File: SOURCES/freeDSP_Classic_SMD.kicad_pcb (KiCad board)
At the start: 2 copper layers, 173 parts, among them J1 RCA_01, J2 RCA_01, J3 CONN_01X02, J4 RCA_01, J5 RCA_01, J6 RCA_01, J7 RCA_01, P1 CONN_01X06, P2 CONN_01X03, P3 CONN_02X05, P4 STDCONN, P5 STDCONN, P6 STDCONN, P7 STDCONN, P8 CONN_02X03, P9 CONN_02X03, Q1 BSS123, Q10 BSH103,215, Q11 BSH103,215, Q12 BSH103,215, Q13 BSH103,215, Q14 MMBF5434, Q15 MMBF5434, Q16 MMBF5434, Q17 MMBF5434, Q18 BSS123, Q2 BSS123, Q3 BSS123, Q4 BSS123, Q5 FZT751TA, Q6 BSH103,215, Q7 BSH103,215, Q8 BSH103,215, Q9 BSH103,215, SW1 SW_PUSH, U1 ADAU1701, U2 24AA256SN, U3 LME49721, U4 LME49721, U5 SN74LVC3G14, U6 LM393, U7 IDT2305NZ, X1 ASV-24.576MHz-EJ-T

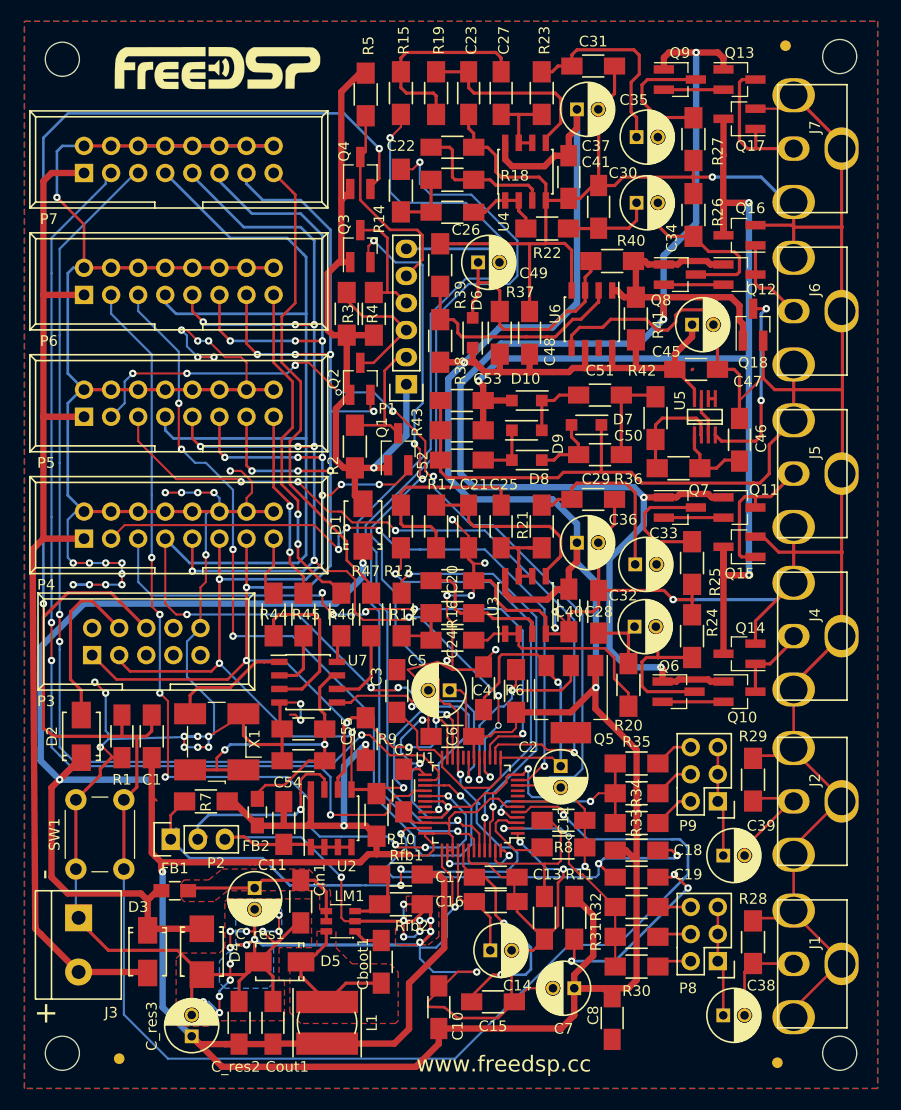
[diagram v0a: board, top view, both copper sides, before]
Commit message: added power led, changed via drill size
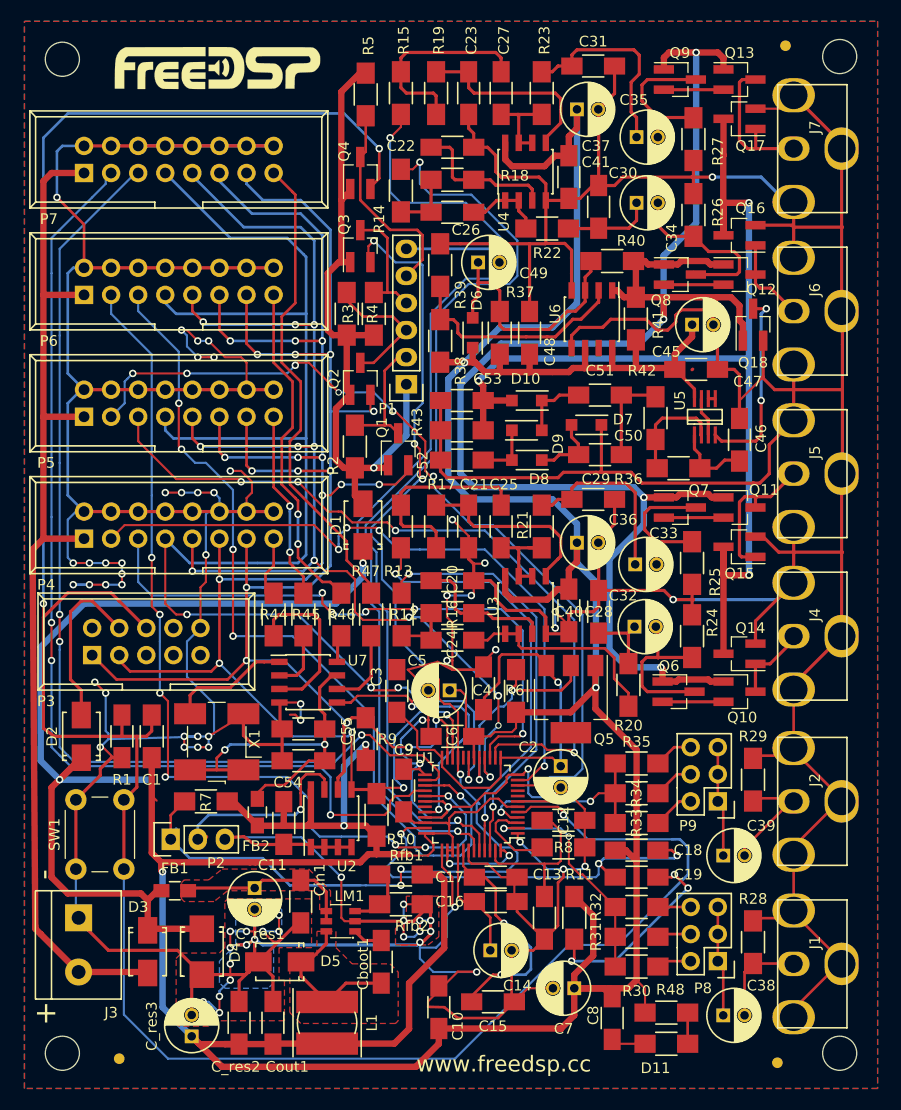
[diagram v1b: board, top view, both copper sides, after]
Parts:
- added D11: LED, fdsp_resistor:R_1206_HandSoldering, F.Cu at (123.7, 153.8)
- added R48: 330, fdsp_resistor:R_1206_HandSoldering, F.Cu at (123.7, 150.9)
- R11: value 475R -> 475
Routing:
- net +3V3: track 422.4 -> 425.7 mm
- net GND: track 1016.5 -> 1019.7 mm
- net Net-(D11-Pad2): track 0.00 -> 2.92 mm
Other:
- net class ADAU: via_drill 0.3 -> 0.4
- net class Default: via_drill 0.3 -> 0.4
- net class Supply: via_drill 0.3 -> 0.4
- rule via_min_size: 0.3 -> 0.4

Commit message: fixed wrong pinouts added some text
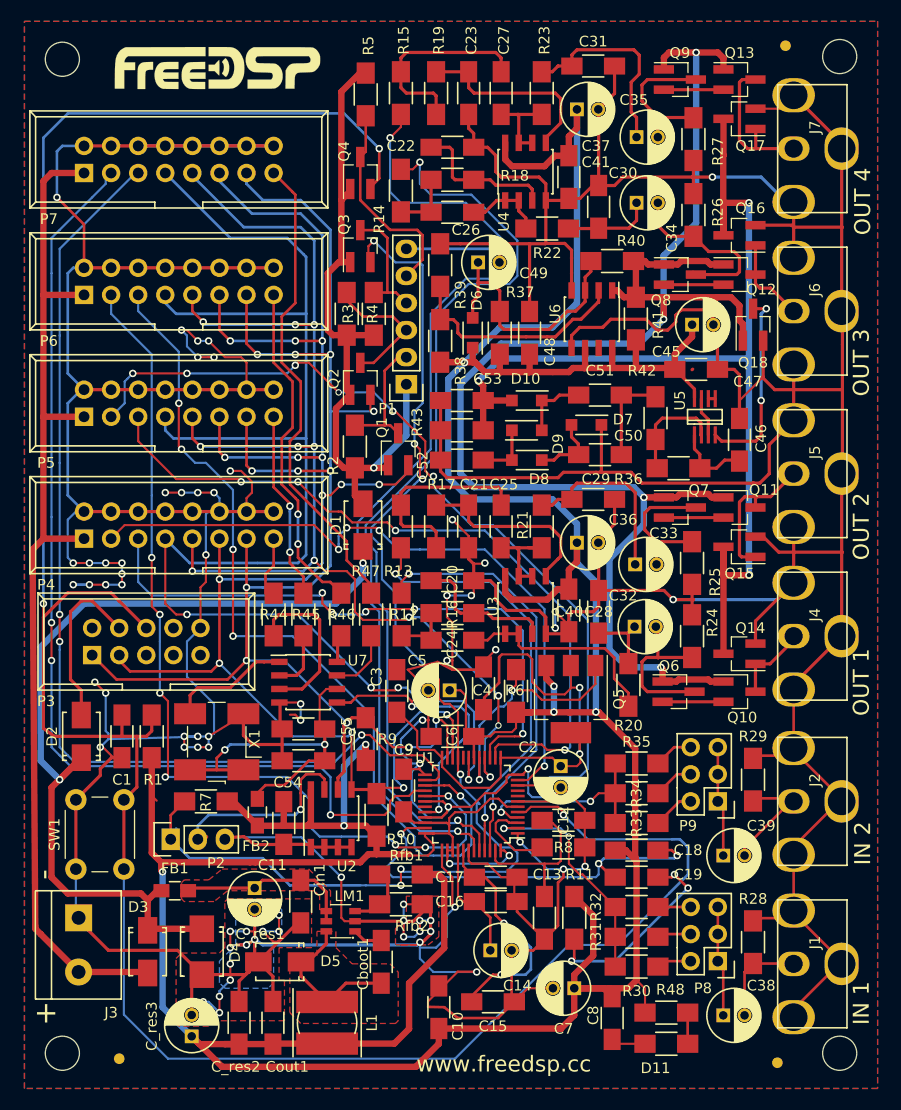
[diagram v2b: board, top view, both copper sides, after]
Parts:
- C28, C29, C30, C31: value 560p -> 5.6n
- Q5: footprint fdsp_housing_new:SOT-223 -> fdsp_housing:SOT-223
- R20, R21, R22, R23: value 2k4 -> 330
- R44, R45, R46, R47: value 33 -> 24
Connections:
- U7 pad 6: Net-(R47-Pad2) -> Net-(C54-Pad1)
- U7 pad 7: Net-(C54-Pad1) -> Net-(R47-Pad2)
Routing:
- net Net-(C2-Pad1): track 43.5 -> 53.8 mm, vias 1 -> 2
- net VIN: track 92.6 -> 84.0 mm
- net +3V3: track 425.7 -> 433.3 mm, vias 7 -> 9
- net Net-(Q5-Pad2): track 22.5 -> 25.3 mm
- net MP7: track 71.4 -> 70.3 mm
- net Net-(C54-Pad1): track 34.3 -> 33.3 mm
- net Net-(R47-Pad2): track 7.46 -> 6.64 mm
- net MP1: track 80.9 -> 81.7 mm
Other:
- board text added: "IN 1"
- board text added: "IN 2"
- board text added: "OUT 1"
- board text added: "OUT 2"
- board text added: "OUT 3"
- board text added: "OUT 4"

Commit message: Modified FZT751 Part2
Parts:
- Q5: footprint fdsp_housing:SOT-223 -> fdsp_housing_new:SOT-223
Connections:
- Q5 pad 1: +3V3 -> Net-(Q5-Pad1)
- Q5 pad 2: Net-(Q5-Pad2) -> (no net)
- Q5 pad 3: Net-(C2-Pad1) -> +3V3
- R6 pad 2: Net-(Q5-Pad2) -> Net-(Q5-Pad1)
- U1 pad 17: Net-(Q5-Pad2) -> Net-(Q5-Pad1)
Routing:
- net Net-(Q5-Pad2): track 25.3 -> 0.00 mm, vias 2 -> 0
- net Net-(Q5-Pad1): track 0.00 -> 25.3 mm, vias 0 -> 2

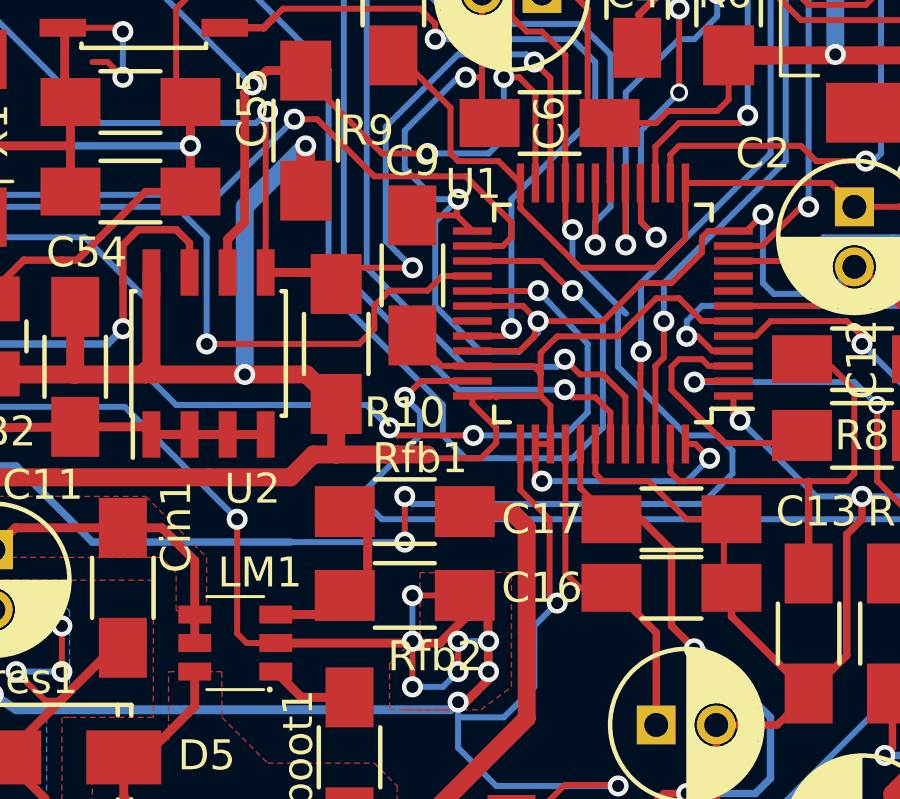
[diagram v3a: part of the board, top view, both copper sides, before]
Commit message: corrected some things in layout and schematic
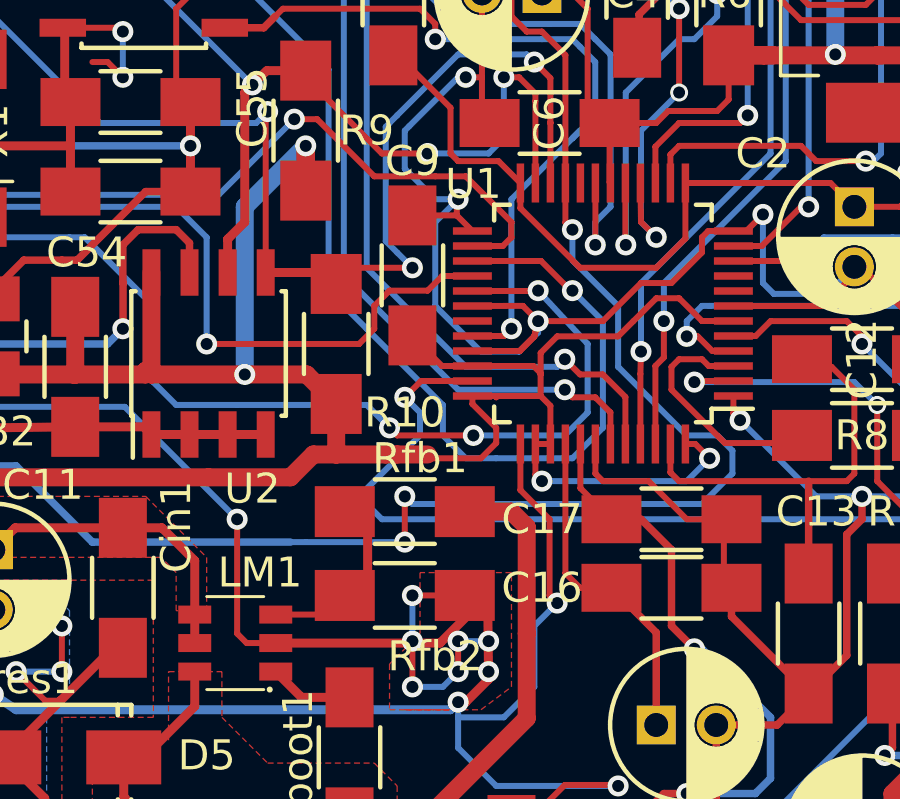
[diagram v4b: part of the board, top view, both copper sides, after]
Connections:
- Q5 pad 2: (no net) -> Net-(C2-Pad1)
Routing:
- net WP: track 115.4 -> 114.7 mm
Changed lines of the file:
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@@
-(kicad_pcb (version 4) (host pcbnew 4.0.7-e1-6374~58~ubuntu17.04.1)
+(kicad_pcb (version 4) (host pcbnew 4.0.7-e1-6374~58~ubuntu16.04.1)
   (general
-    (links 412)
+    (links 414)
     (no_connects 0)
     (area 0 0 0 0)
@@
     (pad_to_mask_clearance 0)
     (aux_axis_origin 0 0)
-    (visible_elements 7FFC0E09)
+    (visible_elements 7FFC4E0F)
     (pcbplotparams
       (layerselection 0x020c0_00000000)
@@
     (uvia_dia 0.3)
     (uvia_drill 0.1)
-    (add_net "Net-(Q5-Pad1)")
   )
   (net_class ADAU ""
@@
     (add_net "Net-(Q12-Pad2)")
     (add_net "Net-(Q13-Pad2)")
+    (add_net "Net-(Q5-Pad1)")
     (add_net "Net-(R36-Pad1)")
     (add_net "Net-(R38-Pad1)")
@@
     (fp_line (start -1.85 3.35) (end 1.85 3.35) (layer F.Fab) (width 0.1))
     (fp_line (start 1.85 -3.35) (end 1.85 3.35) (layer F.Fab) (width 0.1))
-    (pad 4 smd rect (at 3.15 0 270) (size 2 3.8) (layers F.Cu F.Paste F.Mask))
-    (pad 2 smd rect (at -3.15 0 270) (size 2 1.5) (layers F.Cu F.Paste F.Mask))
+    (pad 2 smd rect (at 3.15 0 270) (size 2 3.8) (layers F.Cu F.Paste F.Mask)
+      (net 3 "Net-(C2-Pad1)"))
+    (pad 2 smd rect (at -3.15 0 270) (size 2 1.5) (layers F.Cu F.Paste F.Mask)
+      (net 3 "Net-(C2-Pad1)"))
     (pad 3 smd rect (at -3.15 2.3 270) (size 2 1.5) (layers F.Cu F.Paste F.Mask)
       (net 4 +3V3))
@@
   (segment (start 132.08 69.85) (end 135.636 69.85) (width 0.3) (layer F.Cu) (net 52))
   (segment (start 130.556 69.088) (end 131.318 69.85) (width 0.3) (layer F.Cu) (net 52))
+  (segment (start 94.5045 141.3535) (end 96.1685 141.3535) (width 0.2) (layer F.Cu) (net 53))
+  (segment (start 96.1685 141.3535) (end 96.806 140.716) (width 0.2) (layer F.Cu) (net 53))
   (segment (start 97.568 137.922) (end 97.568 140.716) (width 0.3) (layer F.Cu) (net 53))
-  (segment (start 94.5045 141.3535) (end 97.1845 141.3535) (width 0.3) (layer F.Cu) (net 53))
   (segment (start 97.1845 141.3535) (end 97.5045 141.0335) (width 0.3) (layer F.Cu) (net 53))
   (segment (start 99.314 89.408) (end 98.552 89.408) (width 0.25) (layer F.Cu) (net 54))
@@
   (segment (start 97.79 77.47) (end 100.33 77.47) (width 0.25) (layer F.Cu) (net 57))
   (segment (start 94.996 74.676) (end 97.79 77.47) (width 0.25) (layer F.Cu) (net 57))
-  (segment (start 94.996 138.938) (end 88.392 138.938) (width 0.25) (layer B.Cu) (net 58))
-  (segment (start 78.994 136.398) (end 77.216 134.62) (width 0.25) (layer B.Cu) (net 58))
-  (segment (start 85.852 136.398) (end 78.994 136.398) (width 0.25) (layer B.Cu) (net 58))
-  (segment (start 88.392 138.938) (end 85.852 136.398) (width 0.25) (layer B.Cu) (net 58))
-  (segment (start 98.806 138.938) (end 95.504 138.938) (width 0.2) (layer B.Cu) (net 58))
-  (segment (start 101.092 137.668) (end 99.06 137.668) (width 0.2) (layer B.Cu) (net 58))
-  (segment (start 104.394 129.54) (end 106.172 131.318) (width 0.2) (layer B.Cu) (net 58))
-  (segment (start 106.172 131.318) (end 105.918 131.064) (width 0.2) (layer B.Cu) (net 58))
-  (segment (start 105.918 131.064) (end 105.918 133.096) (width 0.2) (layer B.Cu) (net 58))
-  (segment (start 105.918 133.096) (end 108.204 135.382) (width 0.2) (layer B.Cu) (net 58))
-  (segment (start 108.204 135.382) (end 109.22 135.382) (width 0.2) (layer B.Cu) (net 58))
-  (segment (start 109.22 135.382) (end 109.728 135.89) (width 0.2) (layer B.Cu) (net 58))
-  (segment (start 109.728 135.89) (end 109.728 136.652) (width 0.2) (layer B.Cu) (net 58))
-  (segment (start 109.728 136.652) (end 108.712 137.668) (width 0.2) (layer B.Cu) (net 58))
-  (segment (start 108.712 137.668) (end 101.092 137.668) (width 0.2) (layer B.Cu) (net 58))
-  (segment (start 104.16 128.29) (end 104.16 126.968) (width 0.2) (layer F.Cu) (net 58))
-  (via (at 104.394 128.524) (size 0.7) (drill 0.4) (layers F.Cu B.Cu) (net 58))
-  (segment (start 104.16 128.29) (end 104.394 128.524) (width 0.2) (layer F.Cu) (net 58))
-  (segment (start 104.394 128.524) (end 104.394 129.54) (width 0.2) (layer B.Cu) (net 58))
-  (segment (start 98.806 137.414) (end 98.806 138.938) (width 0.2) (layer F.Cu) (net 58))
-  (via (at 98.806 137.414) (size 0.7) (drill 0.4) (layers F.Cu B.Cu) (net 58))
-  (segment (start 99.06 137.668) (end 98.806 137.414) (width 0.2) (layer B.Cu) (net 58))
-  (via (at 98.806 138.938) (size 0.7) (drill 0.4) (layers F.Cu B.Cu) (net 58))
+  (segment (start 104.394 129.54) (end 105.918 131.064) (width 0.2) (layer B.Cu) (net 58))
   (segment (start 95.504 138.938) (end 94.996 138.938) (width 0.2) (layer B.Cu) (net 58))
+  (via (at 98.806 138.938) (size 0.7) (drill 0.4) (layers F.Cu B.Cu) (net 58))
+  (segment (start 99.06 137.668) (end 98.806 137.414) (width 0.2) (layer B.Cu) (net 58))
+  (via (at 98.806 137.414) (size 0.7) (drill 0.4) (layers F.Cu B.Cu) (net 58))
+  (segment (start 98.806 137.414) (end 98.806 138.938) (width 0.2) (layer F.Cu) (net 58))
+  (segment (start 104.394 128.524) (end 104.394 129.54) (width 0.2) (layer B.Cu) (net 58))
+  (segment (start 104.16 128.29) (end 104.394 128.524) (width 0.2) (layer F.Cu) (net 58))
+  (via (at 104.394 128.524) (size 0.7) (drill 0.4) (layers F.Cu B.Cu) (net 58))
+  (segment (start 104.16 126.968) (end 104.16 128.29) (width 0.2) (layer F.Cu) (net 58))
+  (segment (start 108.712 137.668) (end 101.092 137.668) (width 0.2) (layer B.Cu) (net 58))
+  (segment (start 109.728 136.652) (end 108.712 137.668) (width 0.2) (layer B.Cu) (net 58))
+  (segment (start 109.728 135.89) (end 109.728 136.652) (width 0.2) (layer B.Cu) (net 58))
+  (segment (start 109.22 135.382) (end 109.728 135.89) (width 0.2) (layer B.Cu) (net 58))
+  (segment (start 108.204 135.382) (end 109.22 135.382) (width 0.2) (layer B.Cu) (net 58))
+  (segment (start 105.918 133.096) (end 108.204 135.382) (width 0.2) (layer B.Cu) (net 58))
+  (segment (start 105.918 131.064) (end 105.918 133.096) (width 0.2) (layer B.Cu) (net 58))
+  (segment (start 101.092 137.668) (end 99.06 137.668) (width 0.2) (layer B.Cu) (net 58))
+  (segment (start 98.806 138.938) (end 95.504 138.938) (width 0.2) (layer B.Cu) (net 58))
+  (segment (start 88.392 138.938) (end 85.852 136.398) (width 0.25) (layer B.Cu) (net 58))
+  (segment (start 85.852 136.398) (end 78.994 136.398) (width 0.25) (layer B.Cu) (net 58))
+  (segment (start 78.994 136.398) (end 77.216 134.62) (width 0.25) (layer B.Cu) (net 58))
+  (segment (start 94.996 138.938) (end 88.392 138.938) (width 0.25) (layer B.Cu) (net 58))
   (segment (start 77.724 133.604) (end 77.724 134.112) (width 0.25) (layer B.Cu) (net 58))
   (segment (start 77.724 134.112) (end 77.216 134.62) (width 0.25) (layer B.Cu) (net 58))
